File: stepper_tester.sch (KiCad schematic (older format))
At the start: 9 parts, among them J1 Conn_01x08, J2 Conn_01x08, J3 Conn_01x04, U1 BluePill_STM32F103C

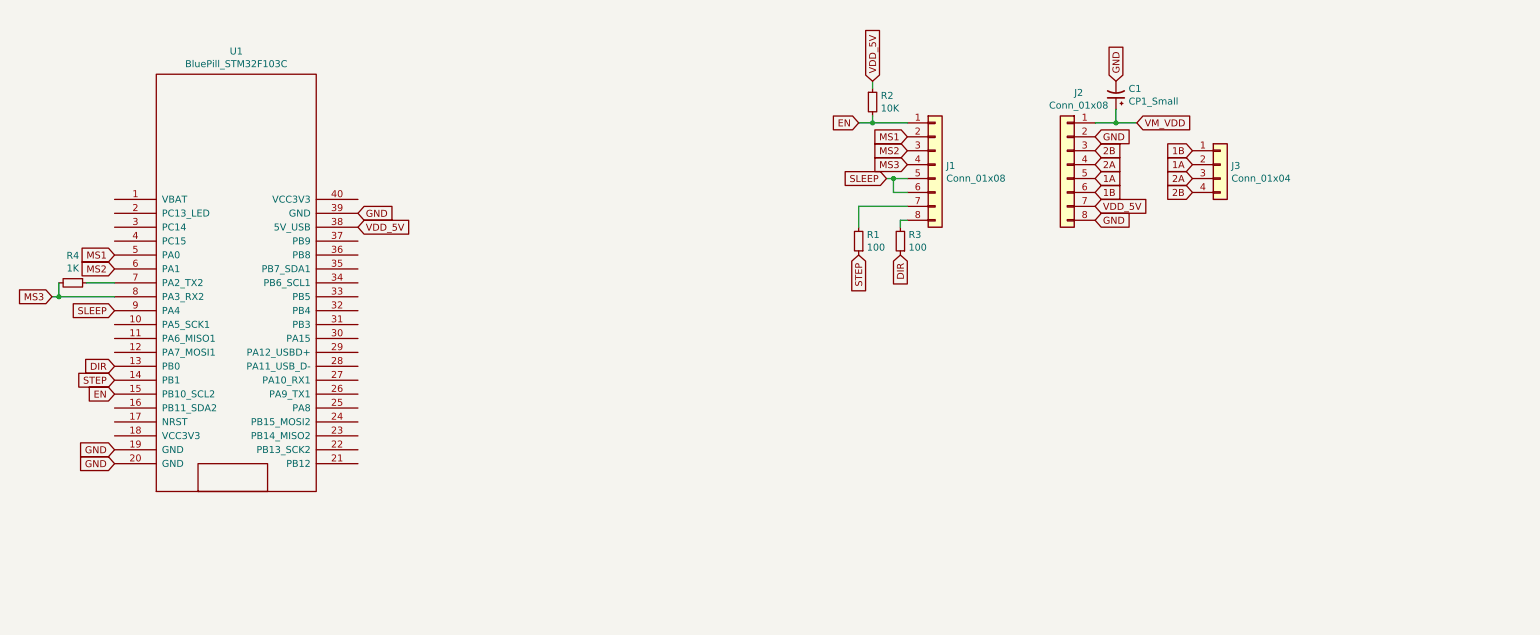
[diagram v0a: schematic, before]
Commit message: Power connector, 90 deg rotation
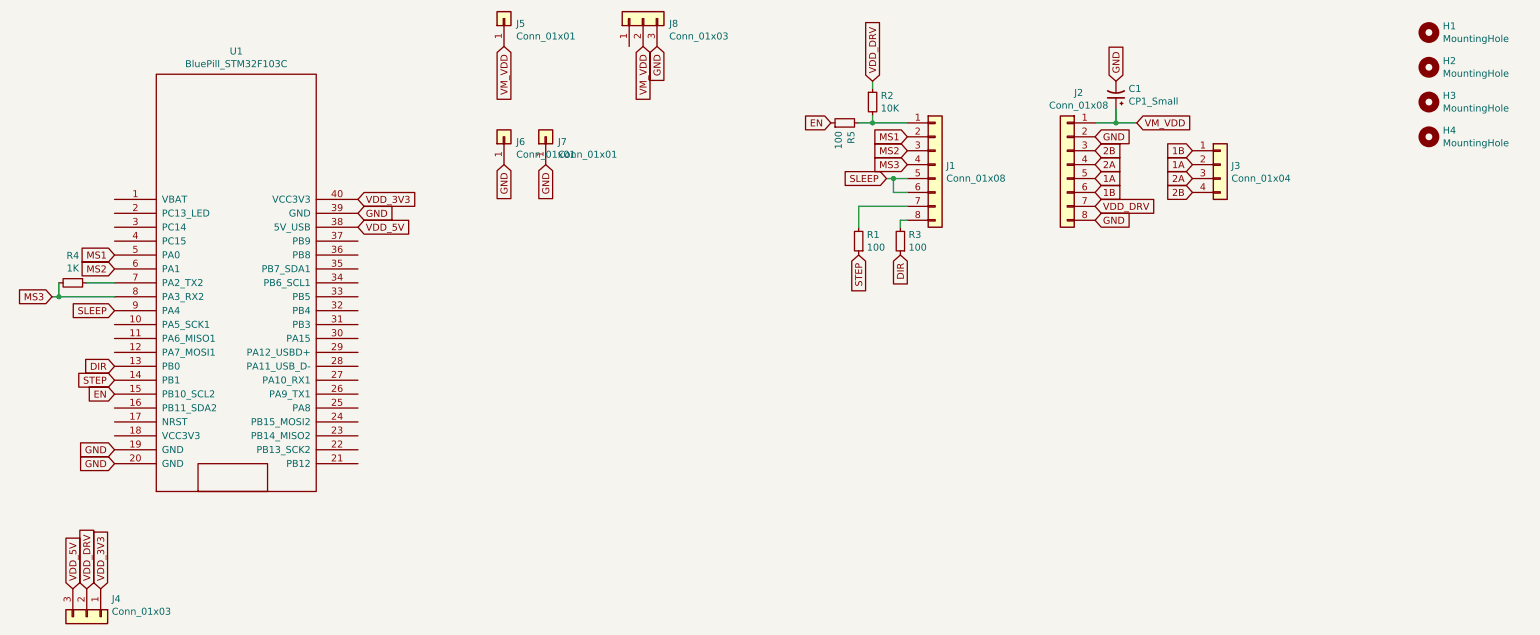
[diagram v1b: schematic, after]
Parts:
- added H1, H2, H3, H4: MountingHole, MountingHole:MountingHole_3.2mm_M3, symbol Mechanical:MountingHole
- added J4: Conn_01x03, Connector_PinHeader_2.54mm:PinHeader_1x03_P2.54mm_Vertical, symbol Connector_Generic:Conn_01x03
- added J5, J6, J7: Conn_01x01, Connector_PinHeader_2.54mm:PinHeader_1x01_P2.54mm_Vertical, symbol Connector_Generic:Conn_01x01
- added J8: Conn_01x03, posad:Socket5.5x2.1, symbol Connector_Generic:Conn_01x03
- added R5: 100, Resistor_SMD:R_0805_2012Metric_Pad1.15x1.40mm_HandSolder, symbol Device:R_Small
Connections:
- net EN: now also R5.1; no longer J1.1 (Pin_1), R2.2
- net GND: now also J6.1 (Pin_1), J7.1 (Pin_1), J8.3 (Pin_3)
- net VDD_5V: now also J4.3 (Pin_3); no longer J2.7 (Pin_7), R2.1
- net VM_VDD: now also J5.1 (Pin_1), J8.2 (Pin_2)
- net VDD_3V3: now reaches U1.40 (VCC3V3)
- net VDD_3V3: now also J4.1 (Pin_1)
- new net: J1.1 (Pin_1), R2.2, R5.2
- new net VDD_DRV: J2.7 (Pin_7), J4.2 (Pin_2), R2.1
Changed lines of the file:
@@
 VDD_5V
 Text GLabel 6800 1200 1    50   Input ~ 0
-VDD_5V
+VDD_DRV
 $Comp
 L Device:R_Small R2
@@
 Wire Wire Line
 	6800 1500 7050 1500
-Text GLabel 6700 1500 0    50   Input ~ 0
+Text GLabel 6500 1500 0    50   Input ~ 0
 EN
 Wire Wire Line
@@
 Text GLabel 9100 1900 0    50   Input ~ 0
 2A
-Text GLabel 8400 2100 2    50   Input ~ 0
-VDD_5V
 Text GLabel 8400 2200 2    50   Input ~ 0
 GND
@@
 Text GLabel 1350 2850 0    50   Input ~ 0
 SLEEP
+$Comp
+L Connector_Generic:Conn_01x03 J4
+U 1 1 5FAF7613
+P 1150 5050
+F 0 "J4" V 1022 5230 50  0000 L CNN
+F 1 "Conn_01x03" V 1113 5230 50  0000 L CNN
+F 2 "Connector_PinHeader_2.54mm:PinHeader_1x03_P2.54mm_Vertical" H 1150 5050 50  0001 C CNN
+F 3 "~" H 1150 5050 50  0001 C CNN
+	1    1150 5050
+	0    1    1    0
+$EndComp
+Text GLabel 8400 2100 2    50   Input ~ 0
+VDD_DRV
+Text GLabel 1150 4850 1    50   Input ~ 0
+VDD_DRV
+Text GLabel 1050 4850 1    50   Input ~ 0
+VDD_5V
+Text GLabel 1250 4850 1    50   Input ~ 0
+VDD_3V3
+$Comp
+L Device:R_Small R5
+U 1 1 5FAF908A
+P 6600 1500
+F 0 "R5" H 6541 1454 50  0000 R CNN
+F 1 "100" H 6541 1545 50  0000 R CNN
+F 2 "Resistor_SMD:R_0805_2012Metric_Pad1.15x1.40mm_HandSolder" H 6600 1500 50  0001 C CNN
+F 3 "~" H 6600 1500 50  0001 C CNN
+	1    6600 1500
+	0    -1   -1   0
+$EndComp
+Text GLabel 3100 2050 2    50   Input ~ 0
+VDD_3V3
+Text GLabel 4150 950  3    50   Input ~ 0
+VM_VDD
+Text GLabel 5250 950  3    50   Input ~ 0
+GND
+$Comp
+L Mechanical:MountingHole H1
+U 1 1 5FAFF5BE
+P 10800 850
+F 0 "H1" H 10900 896 50  0000 L CNN
+F 1 "MountingHole" H 10900 805 50  0000 L CNN
+F 2 "MountingHole:MountingHole_3.2mm_M3" H 10800 850 50  0001 C CNN
+F 3 "~" H 10800 850 50  0001 C CNN
+	1    10800 850
+	1    0    0    -1
+$EndComp
+$Comp
+L Mechanical:MountingHole H2
+U 1 1 5FAFFE89
+P 10800 1100
+F 0 "H2" H 10900 1146 50  0000 L CNN
+F 1 "MountingHole" H 10900 1055 50  0000 L CNN
+F 2 "MountingHole:MountingHole_3.2mm_M3" H 10800 1100 50  0001 C CNN
+F 3 "~" H 10800 1100 50  0001 C CNN
+	1    10800 1100
+	1    0    0    -1
+$EndComp
+$Comp
+L Connector_Generic:Conn_01x03 J8
+U 1 1 5FB06915
+P 5150 750
+F 0 "J8" V 5114 562 50  0000 R CNN
+F 1 "Conn_01x03" V 5023 562 50  0000 R CNN
+F 2 "posad:Socket5.5x2.1" H 5150 750 50  0001 C CNN
+F 3 "~" H 5150 750 50  0001 C CNN
+	1    5150 750
+	0    -1   -1   0
+$EndComp
+Text GLabel 5150 950  3    50   Input ~ 0
+VM_VDD
+$Comp
+L Connector_Generic:Conn_01x01 J5
+U 1 1 5FB07C71
+P 4150 750
+F 0 "J5" V 4114 662 50  0000 R CNN
+F 1 "Conn_01x01" V 4023 662 50  0000 R CNN
+F 2 "Connector_PinHeader_2.54mm:PinHeader_1x01_P2.54mm_Vertical" H 4150 750 50  0001 C CNN
+F 3 "~" H 4150 750 50  0001 C CNN
+	1    4150 750
+	0    -1   -1   0
+$EndComp
+$Comp
+L Connector_Generic:Conn_01x01 J6
+U 1 1 5FB0870B
+P 4150 1600
+F 0 "J6" V 4114 1512 50  0000 R CNN
+F 1 "Conn_01x01" V 4023 1512 50  0000 R CNN
+F 2 "Connector_PinHeader_2.54mm:PinHeader_1x01_P2.54mm_Vertical" H 4150 1600 50  0001 C CNN
+F 3 "~" H 4150 1600 50  0001 C CNN
+	1    4150 1600
+	0    -1   -1   0
+$EndComp
+Text GLabel 4150 1800 3    50   Input ~ 0
+GND
+$Comp
+L Connector_Generic:Conn_01x01 J7
+U 1 1 5FB0933F
+P 4450 1600
+F 0 "J7" V 4414 1512 50  0000 R CNN
+F 1 "Conn_01x01" V 4323 1512 50  0000 R CNN
+F 2 "Connector_PinHeader_2.54mm:PinHeader_1x01_P2.54mm_Vertical" H 4450 1600 50  0001 C CNN
+F 3 "~" H 4450 1600 50  0001 C CNN
+	1    4450 1600
+	0    -1   -1   0
+$EndComp
+Text GLabel 4450 1800 3    50   Input ~ 0
+GND
+$Comp
+L Mechanical:MountingHole H3
+U 1 1 5FB096CF
+P 10800 1350
+F 0 "H3" H 10900 1396 50  0000 L CNN
+F 1 "MountingHole" H 10900 1305 50  0000 L CNN
+F 2 "MountingHole:MountingHole_3.2mm_M3" H 10800 1350 50  0001 C CNN
+F 3 "~" H 10800 1350 50  0001 C CNN
+	1    10800 1350
+	1    0    0    -1
+$EndComp
+$Comp
+L Mechanical:MountingHole H4
+U 1 1 5FB09976
+P 10800 1600
+F 0 "H4" H 10900 1646 50  0000 L CNN
+F 1 "MountingHole" H 10900 1555 50  0000 L CNN
+F 2 "MountingHole:MountingHole_3.2mm_M3" H 10800 1600 50  0001 C CNN
+F 3 "~" H 10800 1600 50  0001 C CNN
+	1    10800 1600
+	1    0    0    -1
+$EndComp
 $EndSCHEMATC

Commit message: Схема
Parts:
- J8: footprint posad:Socket5.5x2.1 -> power:DC55x21THT
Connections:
- net GND: now also J8.2 (Pin_2)
- net VM_VDD: now also J8.1 (Pin_1); no longer J8.2 (Pin_2)
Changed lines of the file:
@@
 F 0 "J8" V 5114 562 50  0000 R CNN
 F 1 "Conn_01x03" V 5023 562 50  0000 R CNN
-F 2 "posad:Socket5.5x2.1" H 5150 750 50  0001 C CNN
+F 2 "power:DC55x21THT" H 5150 750 50  0001 C CNN
 F 3 "~" H 5150 750 50  0001 C CNN
 	1    5150 750
 	0    -1   -1   0
 $EndComp
-Text GLabel 5150 950  3    50   Input ~ 0
+Text GLabel 5050 950  3    50   Input ~ 0
 VM_VDD
 $Comp
@@
 	1    0    0    -1
 $EndComp
+Text GLabel 5150 950  3    50   Input ~ 0
+GND
 $EndSCHEMATC
